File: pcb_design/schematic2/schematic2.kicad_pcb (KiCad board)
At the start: 2 copper layers, 159.5 x 71.5 mm, 29 parts, among them J1 GND | Vcc, J2 I+ | I- | O+ | O- | B+ | B-, J3 R | CC | G | B, SW1 A Button, SW2 B Button, SW3 DPAD UP, SW4 DPAD DOWN, SW5 DPAD LEFT, SW6 DPAD RIGHT, SW7 Opt Button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

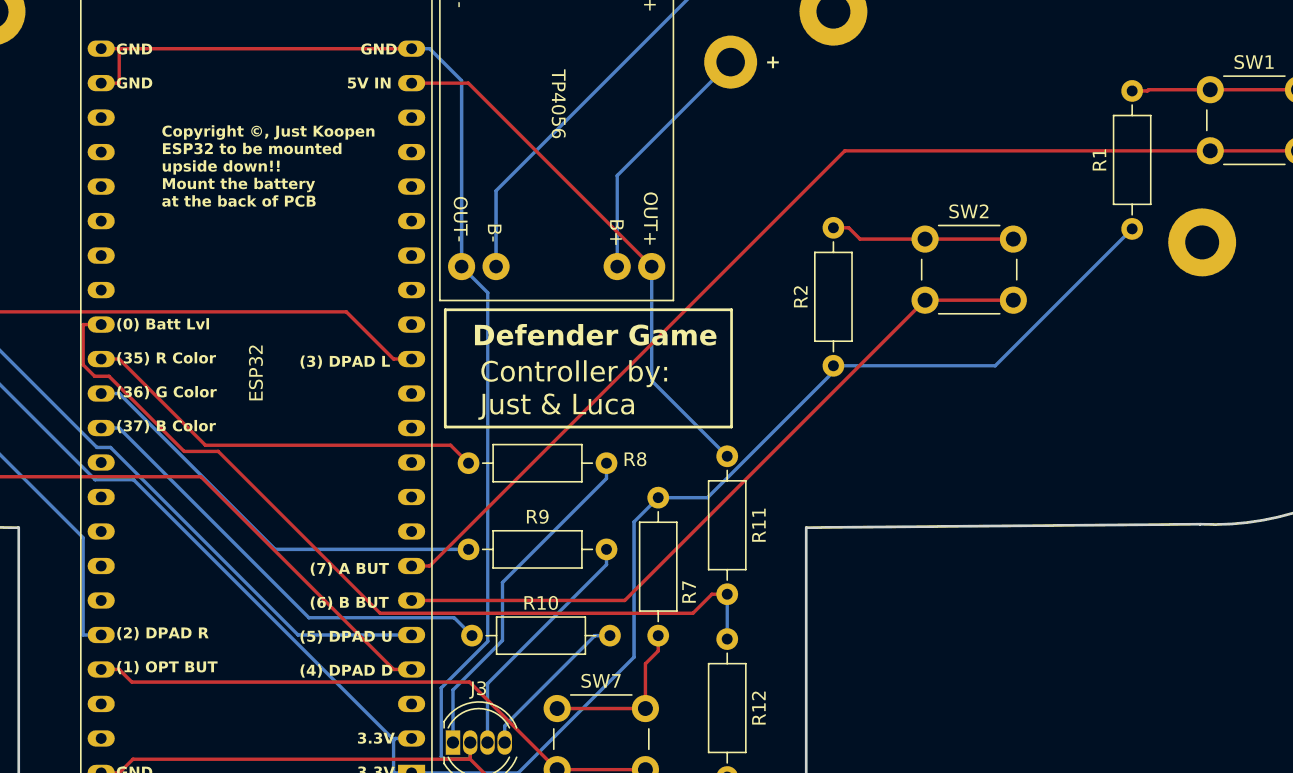
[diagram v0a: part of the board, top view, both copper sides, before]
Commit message: Update schematic2.kicad_sch file
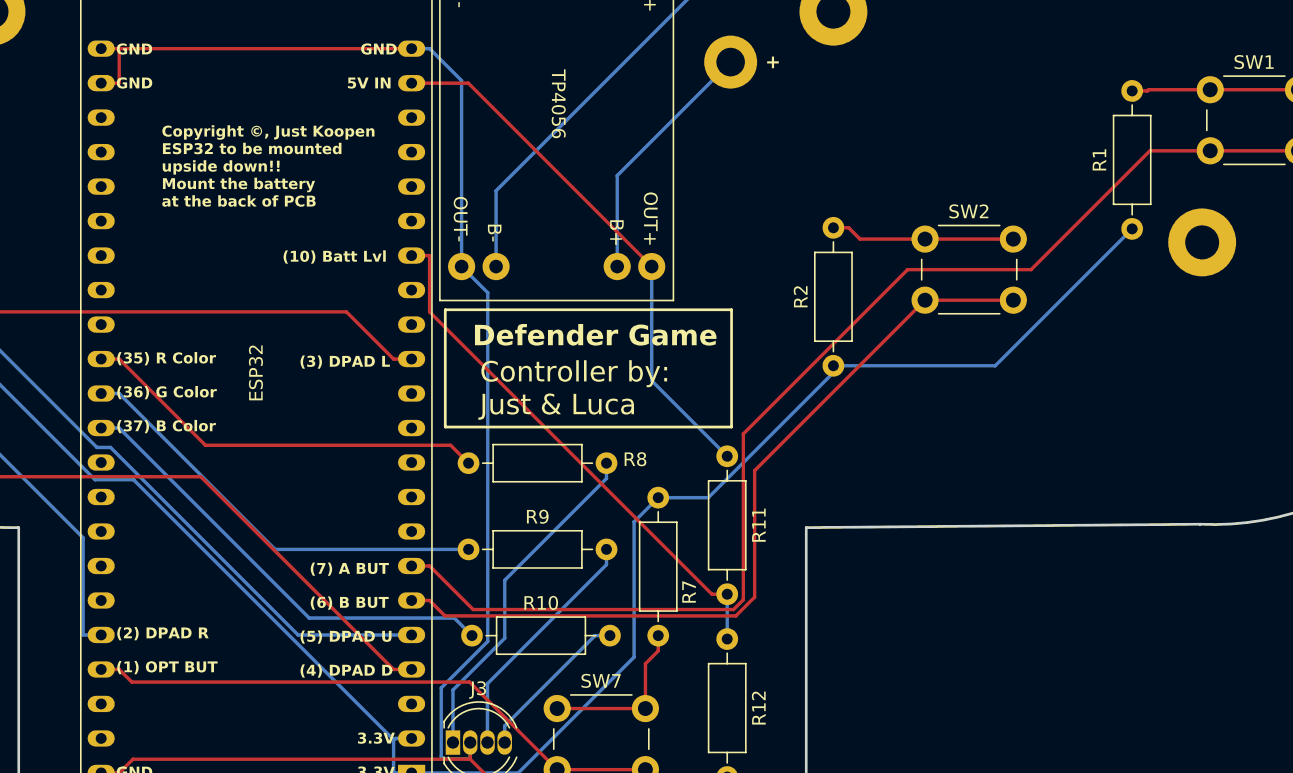
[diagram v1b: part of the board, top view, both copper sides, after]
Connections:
- R11 pad 2: Net-(U1-GPIO0) -> Net-(U1-GPIO10/ADC1_CH9)
- R12 pad 1: Net-(U1-GPIO0) -> Net-(U1-GPIO10/ADC1_CH9)
- U1 pad 16: unconnected-(U1-GPIO10/ADC1_CH9-Pad16) -> Net-(U1-GPIO10/ADC1_CH9)
- U1 pad 31: Net-(U1-GPIO0) -> unconnected-(U1-GPIO0-Pad31)
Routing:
- net Net-(U1-GPIO0): track 63.2 -> 0.00 mm
- net Net-(U1-GPIO10/ADC1_CH9): track 0.00 -> 39.3 mm
- net Net-(U1-GPIO7/ADC1_CH6): track 78.0 -> 87.8 mm
- net Net-(U1-GPIO6/ADC1_CH5): track 53.5 -> 59.9 mm
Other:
- board text added: "(10) Batt Lvl"
- board text removed: "(0) Batt Lvl"

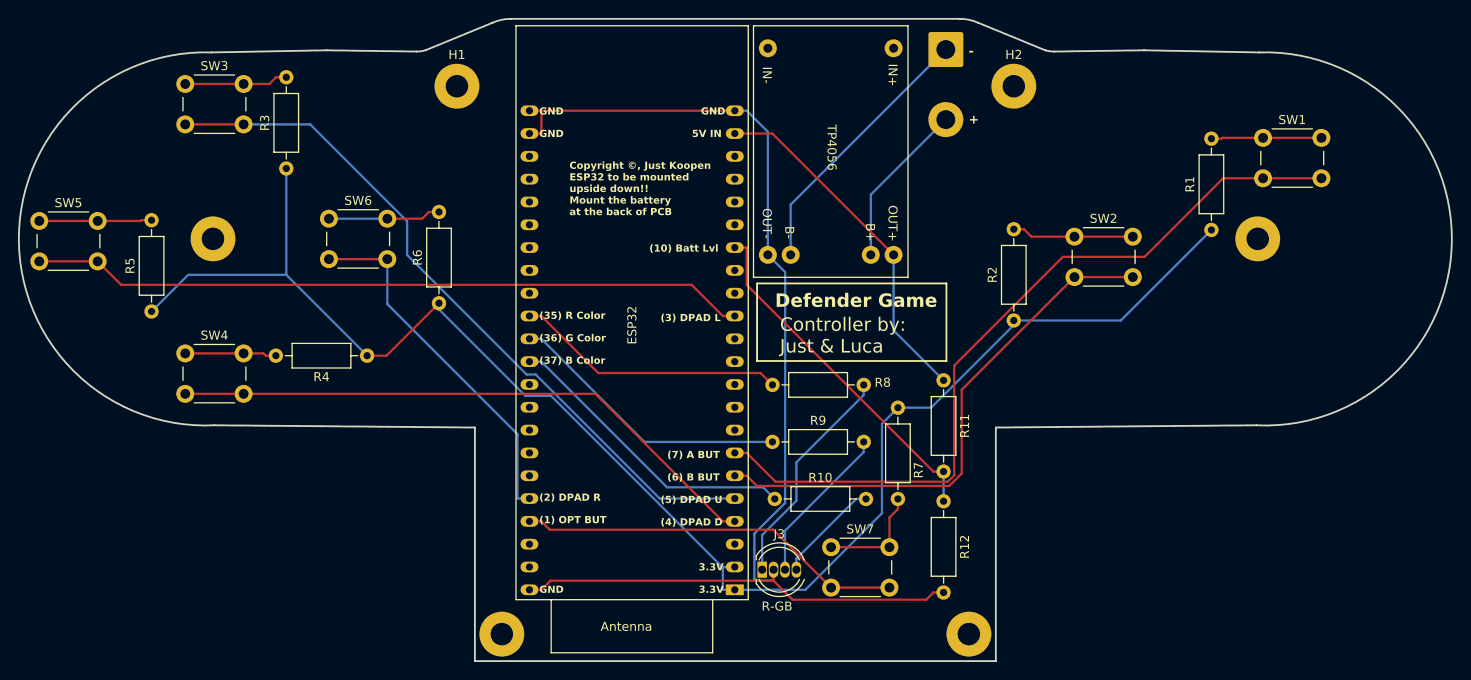
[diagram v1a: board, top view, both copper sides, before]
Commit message: Added switch to PCB design and fixed battery readings
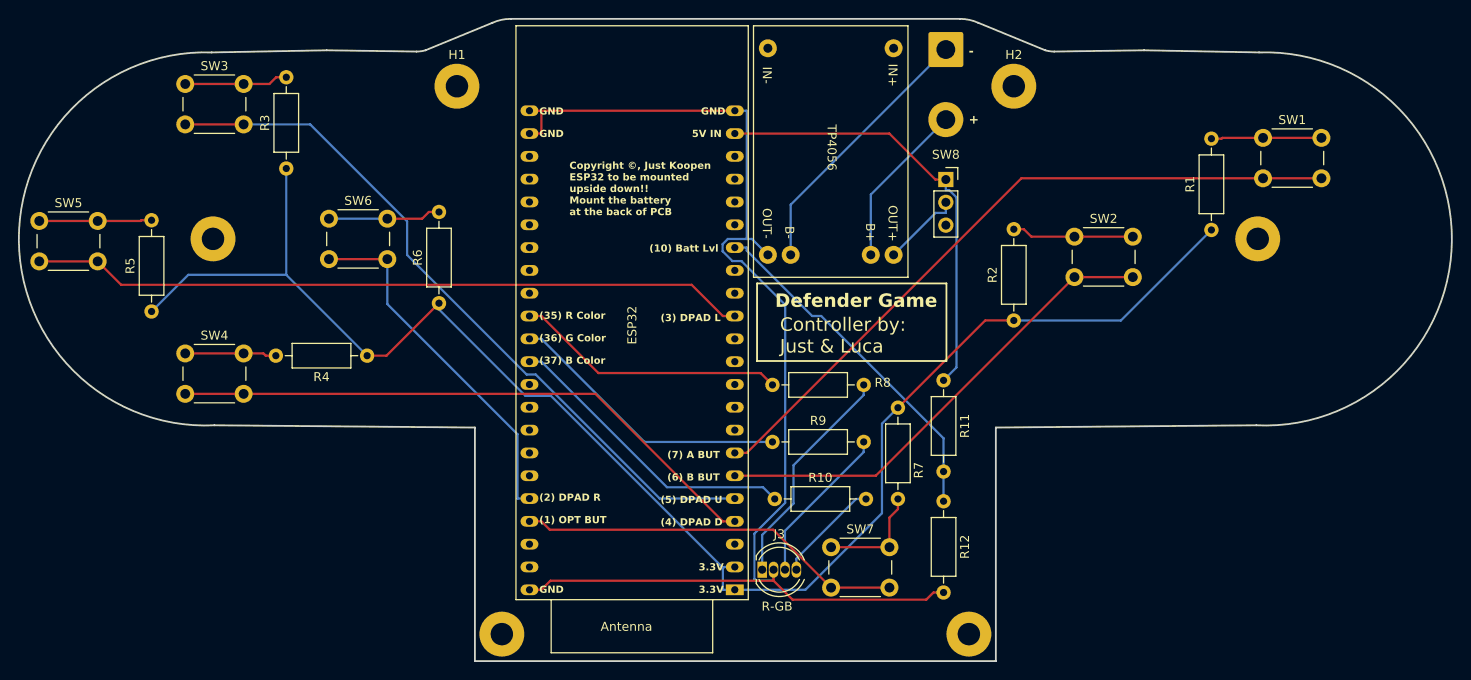
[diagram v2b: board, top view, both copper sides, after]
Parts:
- added SW8: ON / OFF, Connector_PinSocket_2.54mm:PinSocket_1x03_P2.54mm_Vertical, F.Cu at (128.3, 40.4)
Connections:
- R11 pad 1: Net-(J2-Pin_3) -> Net-(SW8-A)
- U1 pad 21: Net-(J2-Pin_3) -> Net-(SW8-A)
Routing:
- net Net-(SW8-A): track 0.00 -> 49.3 mm
- net Net-(J2-Pin_3): track 39.5 -> 8.93 mm
- net Net-(U1-GPIO7/ADC1_CH6): track 87.8 -> 78.0 mm
- net Net-(J2-Pin_4): track 135.8 -> 142.9 mm
- net Net-(U1-GPIO6/ADC1_CH5): track 59.9 -> 53.5 mm

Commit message: kicad files
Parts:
- removed H5, H6: MountingHole, MountingHole:MountingHole_2.5mm_Pad
- added J4: +3.3 LEFT, MountingHole:MountingHole_2.5mm_Pad, F.Cu at (46.7, 47.0)
- added J5: +3.3 RIGHT, MountingHole:MountingHole_2.5mm_Pad, F.Cu at (163.0, 47.0)
- U1: footprint PCM_Espressif:ESP32-S3-DevKitC -> PCM_Espressif:ESP32S3_Dev_Module
- moved U1 8.29 mm to (104.7, 77.8)
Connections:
- J2 pad 4: Net-(J2-Pin_4) -> Net-(J1-Pin_1)
- J3 pad 2: Net-(J2-Pin_4) -> Net-(J1-Pin_1)
- R11 pad 2: Net-(U1-GPIO10/ADC1_CH9) -> Net-(U1-GPIO5/ADC1_CH4)
- R12 pad 1: Net-(U1-GPIO10/ADC1_CH9) -> Net-(U1-GPIO5/ADC1_CH4)
- R12 pad 2: Net-(J2-Pin_4) -> Net-(J1-Pin_1)
- SW3 pad 2: Net-(U1-GPIO5/ADC1_CH4) -> Net-(U1-GPIO21)
- SW4 pad 2: Net-(U1-GPIO4/ADC1_CH3) -> Net-(U1-GPIO42/MTMS)
- SW5 pad 2: Net-(U1-GPIO3/ADC1_CH2) -> Net-(U1-GPIO38)
- SW6 pad 2: Net-(U1-GPIO2/ADC1_CH1) -> Net-(U1-GPIO45)
- SW7 pad 2: Net-(U1-GPIO1/ADC1_CH0) -> Net-(U1-GPIO4/ADC1_CH3)
- U1 pad 13: Net-(U1-GPIO3/ADC1_CH2) -> unconnected-(U1-GPIO3/ADC1_CH2-Pad13)
- U1 pad 16: Net-(U1-GPIO10/ADC1_CH9) -> unconnected-(U1-GPIO10/ADC1_CH9-Pad16)
- U1 pad 22: Net-(J2-Pin_4) -> Net-(J1-Pin_1)
- U1 pad 23: Net-(J2-Pin_4) -> Net-(J1-Pin_1)
- U1 pad 24: Net-(J2-Pin_4) -> Net-(J1-Pin_1)
- U1 pad 27: unconnected-(U1-GPIO21-Pad27) -> Net-(U1-GPIO21)
- U1 pad 30: unconnected-(U1-GPIO45-Pad30) -> Net-(U1-GPIO45)
- U1 pad 35: unconnected-(U1-GPIO38-Pad35) -> Net-(U1-GPIO38)
- U1 pad 39: unconnected-(U1-GPIO42/MTMS-Pad39) -> Net-(U1-GPIO42/MTMS)
- U1 pad 40: Net-(U1-GPIO2/ADC1_CH1) -> unconnected-(U1-GPIO2/ADC1_CH1-Pad40)
- U1 pad 41: Net-(U1-GPIO1/ADC1_CH0) -> unconnected-(U1-GPIO1/ADC1_CH0-Pad41)
- U1 pad 44: Net-(J2-Pin_4) -> Net-(J1-Pin_1)
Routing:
- net Net-(J2-Pin_4): track 142.9 -> 0.00 mm
- net Net-(J1-Pin_1): track 30.0 -> 163.2 mm
- net Net-(U1-GPIO3/ADC1_CH2): track 80.0 -> 0.00 mm
- net Net-(U1-GPIO38): track 0.00 -> 55.4 mm
- net Net-(U1-GPIO5/ADC1_CH4): track 80.6 -> 33.4 mm
- net Net-(U1-GPIO1/ADC1_CH0): track 43.1 -> 0.00 mm
- net Net-(U1-GPIO2/ADC1_CH1): track 40.5 -> 0.00 mm
- net Net-(U1-GPIO10/ADC1_CH9): track 39.2 -> 0.00 mm
- net Net-(U1-GPIO42/MTMS): track 0.00 -> 37.0 mm
- net Net-(U1-GPIO21): track 0.00 -> 36.8 mm
- net Net-(U1-GPIO4/ADC1_CH3): track 67.1 -> 31.9 mm
- net Net-(U1-GPIO45): track 0.00 -> 23.5 mm
- net Net-(SW8-A): track 49.3 -> 60.6 mm
- net Net-(U1-GPIO37): track 33.6 -> 40.7 mm
- net Net-(J4-Pin_1): track 176.5 -> 169.6 mm
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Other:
- board text added: "(21) DPAD U"
- board text added: "(38) DPAD L"
- board text added: "(4) OPT BUT"
- board text added: "(42) DPAD D"
- board text added: "(45) DPAD R"
- board text added: "(5) Batt Lvl"
- board text removed: "(1) OPT BUT"
- board text removed: "(10) Batt Lvl"
- board text removed: "(2) DPAD R"
- board text removed: "(3) DPAD L"
- board text removed: "(4) DPAD D"
- board text removed: "(5) DPAD U"
